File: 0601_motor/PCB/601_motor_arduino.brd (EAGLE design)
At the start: 68.6 x 53.3 mm, 45 parts, among them P1 POLYSWITCHMF-NSML1, SW1 RESET

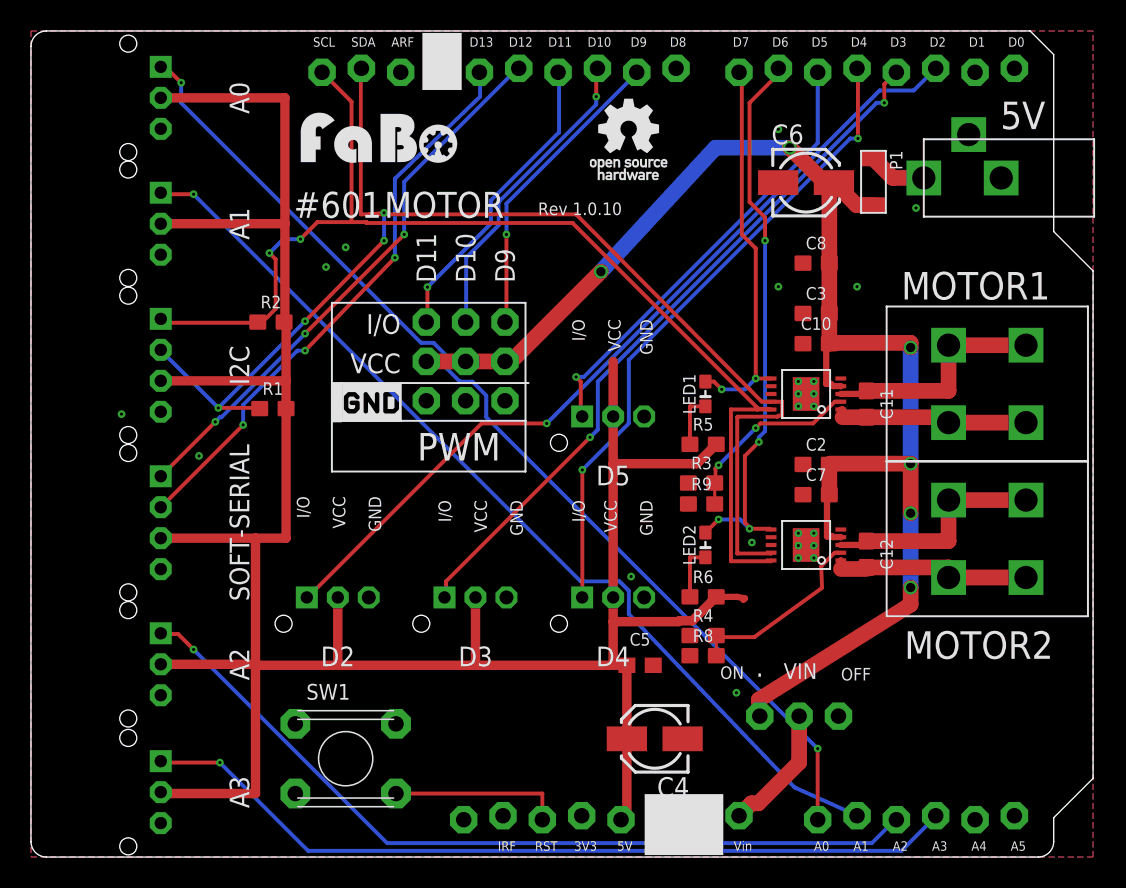
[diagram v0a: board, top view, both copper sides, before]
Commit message: Update lora and Motor.
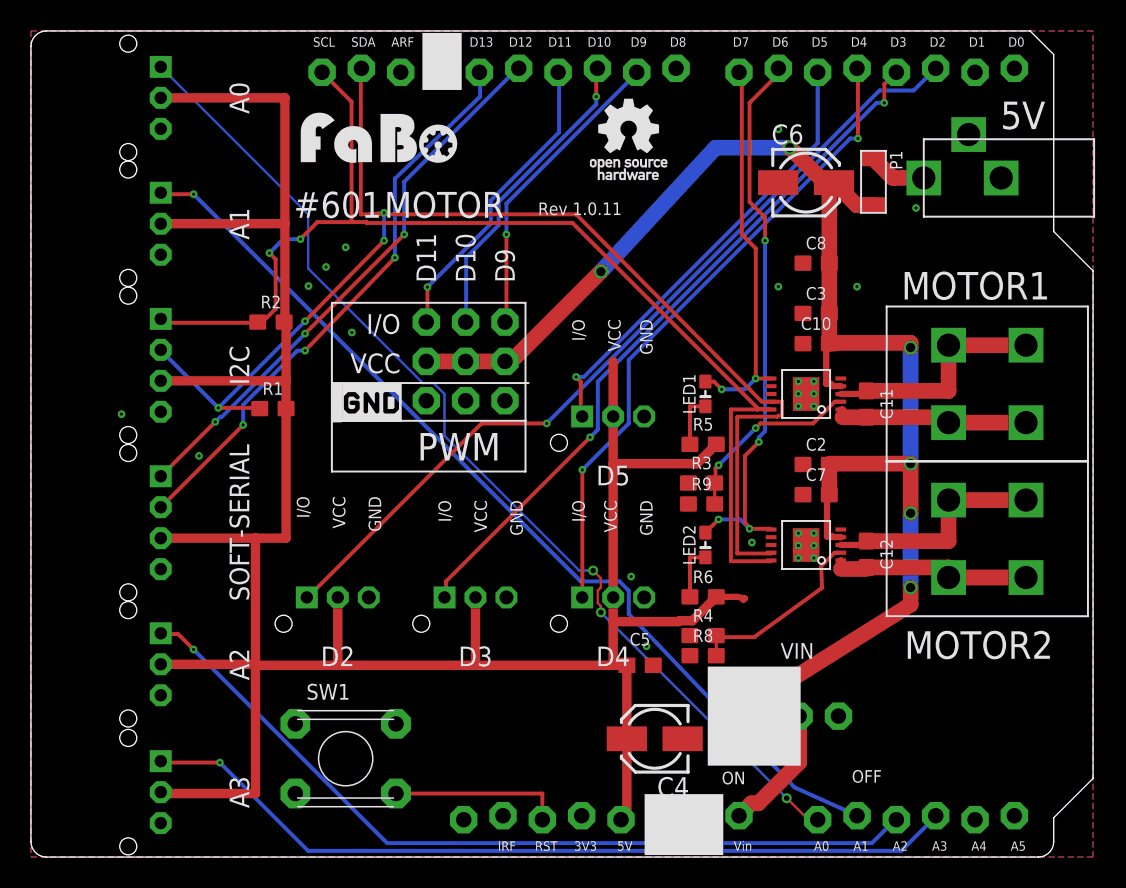
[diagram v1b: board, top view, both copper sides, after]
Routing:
- net A0: track 67.3 -> 67.7 mm, vias 2 -> 3
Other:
- board text added: "Rev 1.0.11"
- board text removed: "Rev 1.0.10"
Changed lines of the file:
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@@
 <wire x1="20.066" y1="30.607" x2="20.066" y2="28.167" width="0.127" layer="21"/>
 <wire x1="31.931" y1="35.787" x2="31.931" y2="28.167" width="0.127" layer="21"/>
-<text x="32.7406" y="41.4528" size="0.8128" layer="21">Rev 1.0.10</text>
+<text x="32.7406" y="41.4528" size="0.8128" layer="21">Rev 1.0.11</text>
 <text x="24.9428" y="25.6032" size="1.778" layer="21">PWM</text>
 <text x="16.9672" y="41.275" size="1.6764" layer="21">#601</text>
@@
 <text x="56.4" y="12.8" size="1.778" layer="21">MOTOR2</text>
 <wire x1="31.931" y1="28.167" x2="31.931" y2="24.892" width="0.127" layer="21"/>
-<text x="44.5" y="11.5" size="0.8128" layer="21">ON</text>
-<text x="52.3" y="11.4" size="0.8128" layer="21">OFF</text>
-<text x="48.6" y="11.5" size="1.016" layer="21">VIN</text>
+<text x="44.6" y="4.7" size="0.8128" layer="21">ON</text>
+<text x="53" y="4.8" size="0.8128" layer="21">OFF</text>
+<text x="48.4" y="12.8" size="1.016" layer="21">VIN</text>
 <text x="62.6" y="47" size="1.778" layer="21">5V</text>
+<rectangle x1="43.7" y1="5.9" x2="49.7" y2="12.3" layer="21"/>
 </plain>
 <attributes>
@@
 <contactref element="R9" pad="1"/>
 <contactref element="U$10" pad="7"/>
+<via x="17.92" y="36.87" extent="1-16" drill="0.2"/>
+<via x="20.72" y="33.87" extent="1-16" drill="0.2"/>
+<via x="39.75" y="13.61" extent="1-16" drill="0.2"/>
 </signal>
 <signal name="5V">
@@
 <contactref element="A0" pad="I/O"/>
 <contactref element="U1" pad="A0"/>
-<wire x1="8.7" y1="51" x2="8.4" y2="51" width="0.254" layer="1"/>
-<wire x1="9.7" y1="50" x2="8.7" y2="51" width="0.254" layer="1"/>
-<wire x1="9.7" y1="48.7" x2="9.7" y2="50" width="0.254" layer="16"/>
-<wire x1="25.2" y1="33.2" x2="9.7" y2="48.7" width="0.254" layer="16"/>
-<wire x1="26" y1="33.2" x2="25.2" y2="33.2" width="0.254" layer="16"/>
-<wire x1="26.8" y1="32.4" x2="26" y2="33.2" width="0.254" layer="16"/>
-<wire x1="26.8" y1="31.6" x2="26.8" y2="32.4" width="0.254" layer="16"/>
-<wire x1="27.7" y1="30.7" x2="26.8" y2="31.6" width="0.254" layer="16"/>
-<wire x1="28.5" y1="30.7" x2="27.7" y2="30.7" width="0.254" layer="16"/>
-<wire x1="29.4" y1="29.8" x2="28.5" y2="30.7" width="0.254" layer="16"/>
-<wire x1="29.4" y1="28.4" x2="29.4" y2="29.8" width="0.254" layer="16"/>
-<wire x1="50.8" y1="7" x2="29.4" y2="28.4" width="0.254" layer="16"/>
-<wire x1="50.8" y1="2.413" x2="50.8" y2="7" width="0.254" layer="1"/>
-<wire x1="8.4" y1="51" x2="8.382" y2="51.022" width="0.254" layer="1"/>
-<via x="9.7" y="50" extent="1-16" drill="0.2"/>
-<via x="50.8" y="7" extent="1-16" drill="0.2"/>
+<wire x1="50.1" y1="2.5" x2="50.8" y2="2.5" width="0.1524" layer="1"/>
+<wire x1="48.8" y1="3.8" x2="50.1" y2="2.5" width="0.1524" layer="1"/>
+<wire x1="36.8" y1="15.8" x2="48.8" y2="3.8" width="0.1524" layer="16"/>
+<wire x1="36.8" y1="16.2" x2="36.8" y2="15.8" width="0.1524" layer="1"/>
+<wire x1="36.6" y1="16.4" x2="36.8" y2="16.2" width="0.1524" layer="1"/>
+<wire x1="36.6" y1="17.2" x2="36.6" y2="16.4" width="0.1524" layer="1"/>
+<wire x1="36.8" y1="17.4" x2="36.6" y2="17.2" width="0.1524" layer="1"/>
+<wire x1="36.8" y1="18" x2="36.8" y2="17.4" width="0.1524" layer="1"/>
+<wire x1="36.3" y1="18.5" x2="36.8" y2="18" width="0.1524" layer="1"/>
+<wire x1="35.4" y1="18.5" x2="36.3" y2="18.5" width="0.1524" layer="16"/>
+<wire x1="26.7" y1="27.2" x2="35.4" y2="18.5" width="0.1524" layer="16"/>
+<wire x1="26.7" y1="29.9" x2="26.7" y2="27.2" width="0.1524" layer="16"/>
+<wire x1="26" y1="30.6" x2="26.7" y2="29.9" width="0.1524" layer="16"/>
+<wire x1="25.3" y1="30.6" x2="26" y2="30.6" width="0.1524" layer="16"/>
+<wire x1="17.9" y1="38" x2="25.3" y2="30.6" width="0.1524" layer="16"/>
+<wire x1="17.9" y1="41.5" x2="17.9" y2="38" width="0.1524" layer="16"/>
+<wire x1="8.4" y1="51" x2="17.9" y2="41.5" width="0.1524" layer="16"/>
+<wire x1="50.8" y1="2.5" x2="50.8" y2="2.413" width="0.1524" layer="1"/>
+<wire x1="8.4" y1="51" x2="8.382" y2="51.022" width="0.1524" layer="16"/>
+<via x="48.8" y="3.8" extent="1-16" drill="0.35"/>
+<via x="36.8" y="15.8" extent="1-16" drill="0.35"/>
+<via x="36.3" y="18.5" extent="1-16" drill="0.35"/>
 </signal>
 <signal name="D13">

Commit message: #601 motor　ロゴ修正
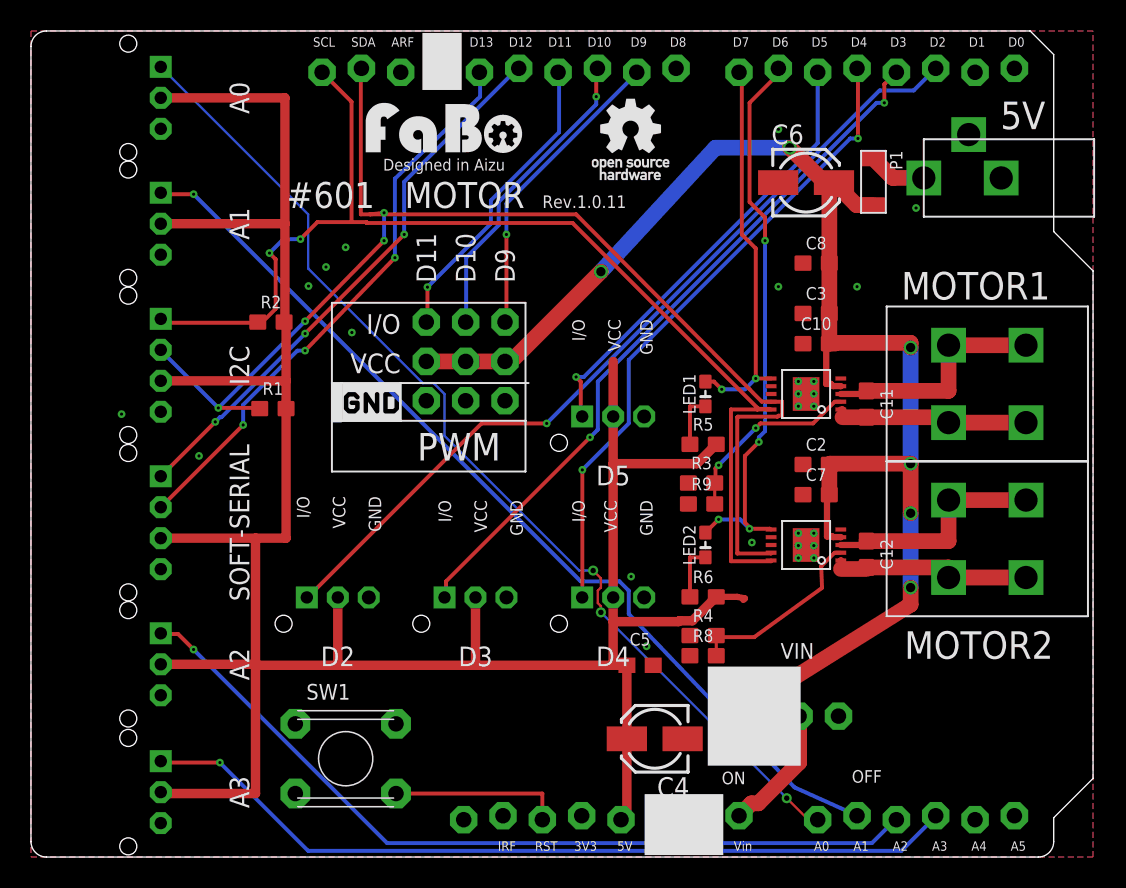
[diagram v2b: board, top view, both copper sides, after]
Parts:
- removed U$7: (no value), FaBo-etc:LOGO_FABO_MS
- added LOGO1: (no value), component:LOGO_FABO_M
- moved U$6 0.13 mm to (38.7, 47.0)
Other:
- board text added: "Designed in Aizu"
- board text added: "Rev.1.0.11"
- board text removed: "Rev 1.0.11"
